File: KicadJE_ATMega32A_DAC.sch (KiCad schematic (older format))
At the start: 74 parts, among them J101 CV1, J102 CV2, J103 OUT1, J104 OUT2, J105 IN1, J106 IN2

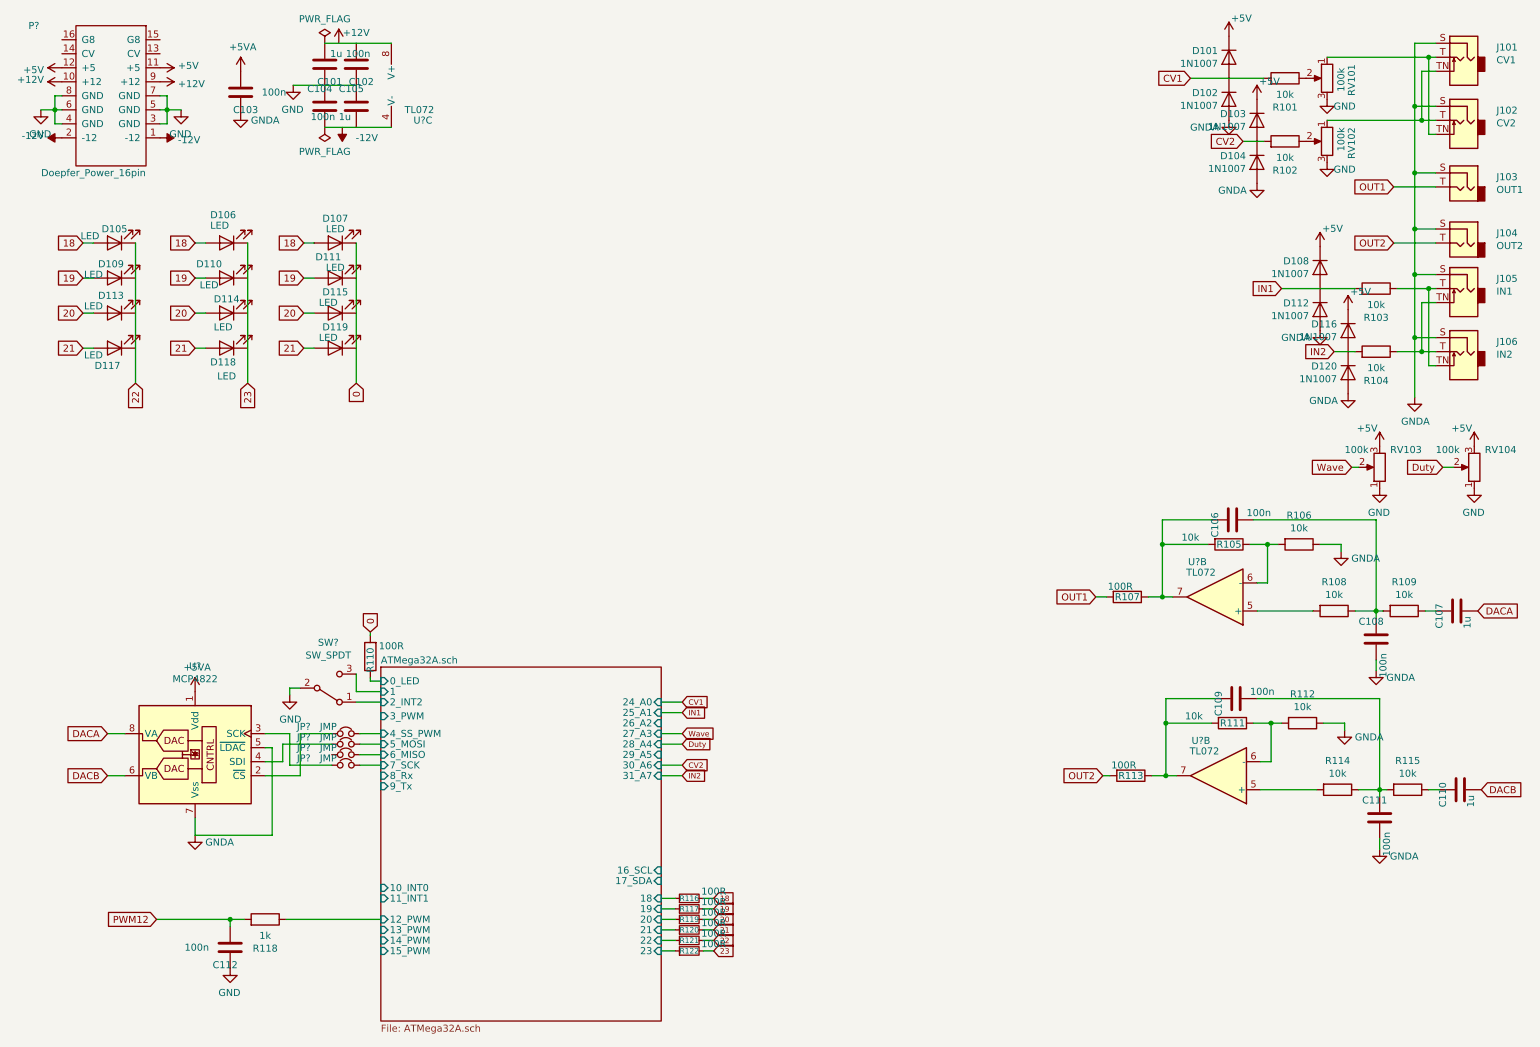
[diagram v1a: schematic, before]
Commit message: Intersheet cleanup
Footprints and cleanup naming on global labels between sheets
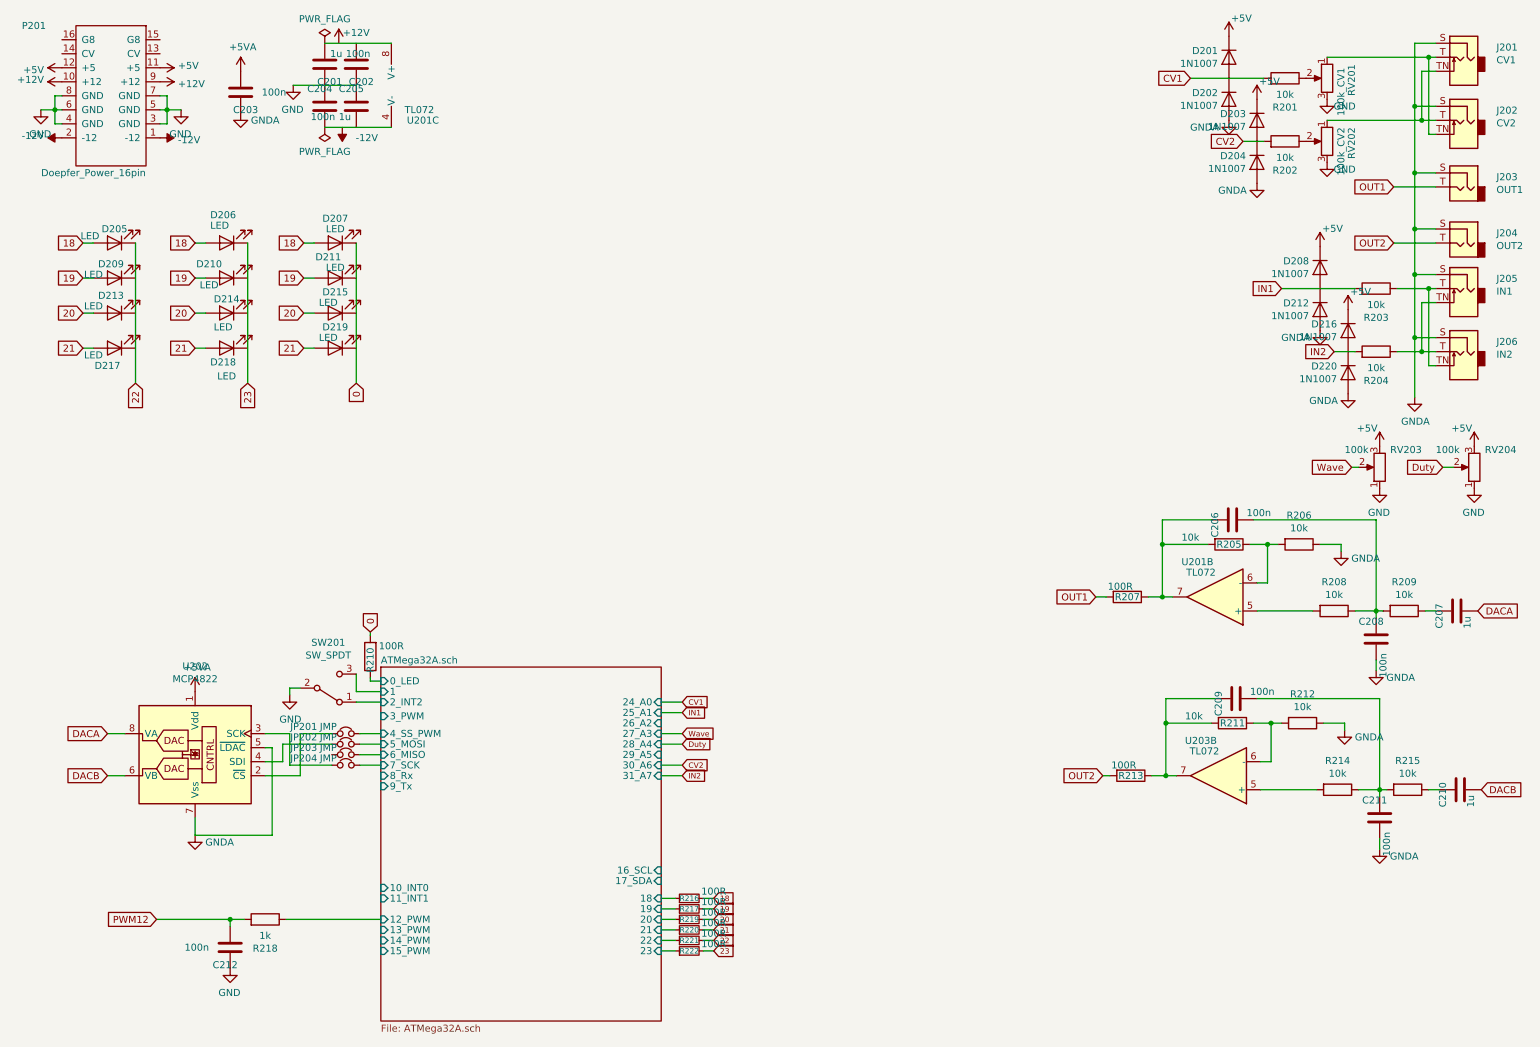
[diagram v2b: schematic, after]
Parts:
- RV201: renamed from RV101; value 100k -> 100k_CV1
- RV202: renamed from RV102; value 100k -> 100k_CV2
- SW201: renamed from SW?; footprint (none) -> AJ:SP1MS1
- U201, U202, U203: renamed from U?; footprint (none) -> AJ:AJ_SO-8_5.3x6.2mm_P1.27mm
- gave numbers to parts that had none: 6
- renumbered C101 to C201, C102 to C202, C103 to C203, C104 to C204, C105 to C205, C106 to C206, C107 to C207, C108 to C208, C109 to C209, C110 to C210, C111 to C211, C112 to C212, D101 to D201, D102 to D202, D103 to D203, D104 to D204, D105 to D205, D106 to D206, D107 to D207, D108 to D208, D109 to D209, D110 to D210, D111 to D211, D112 to D212, D113 to D213, D114 to D214, D115 to D215, D116 to D216, D117 to D217, D118 to D218, D119 to D219, D120 to D220, J101 to J201, J102 to J202, J103 to J203, J104 to J204, J105 to J205, J106 to J206, R101 to R201, R102 to R202, R103 to R203, R104 to R204, R105 to R205, R106 to R206, R107 to R207, R108 to R208, R109 to R209, R110 to R210, R111 to R211, R112 to R212, R113 to R213, R114 to R214, R115 to R215, R116 to R216, R117 to R217, R118 to R218, R119 to R219, R120 to R220, R121 to R221, R122 to R222, RV103 to RV203, RV104 to RV204

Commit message: LED Matrix ATMega32 rename
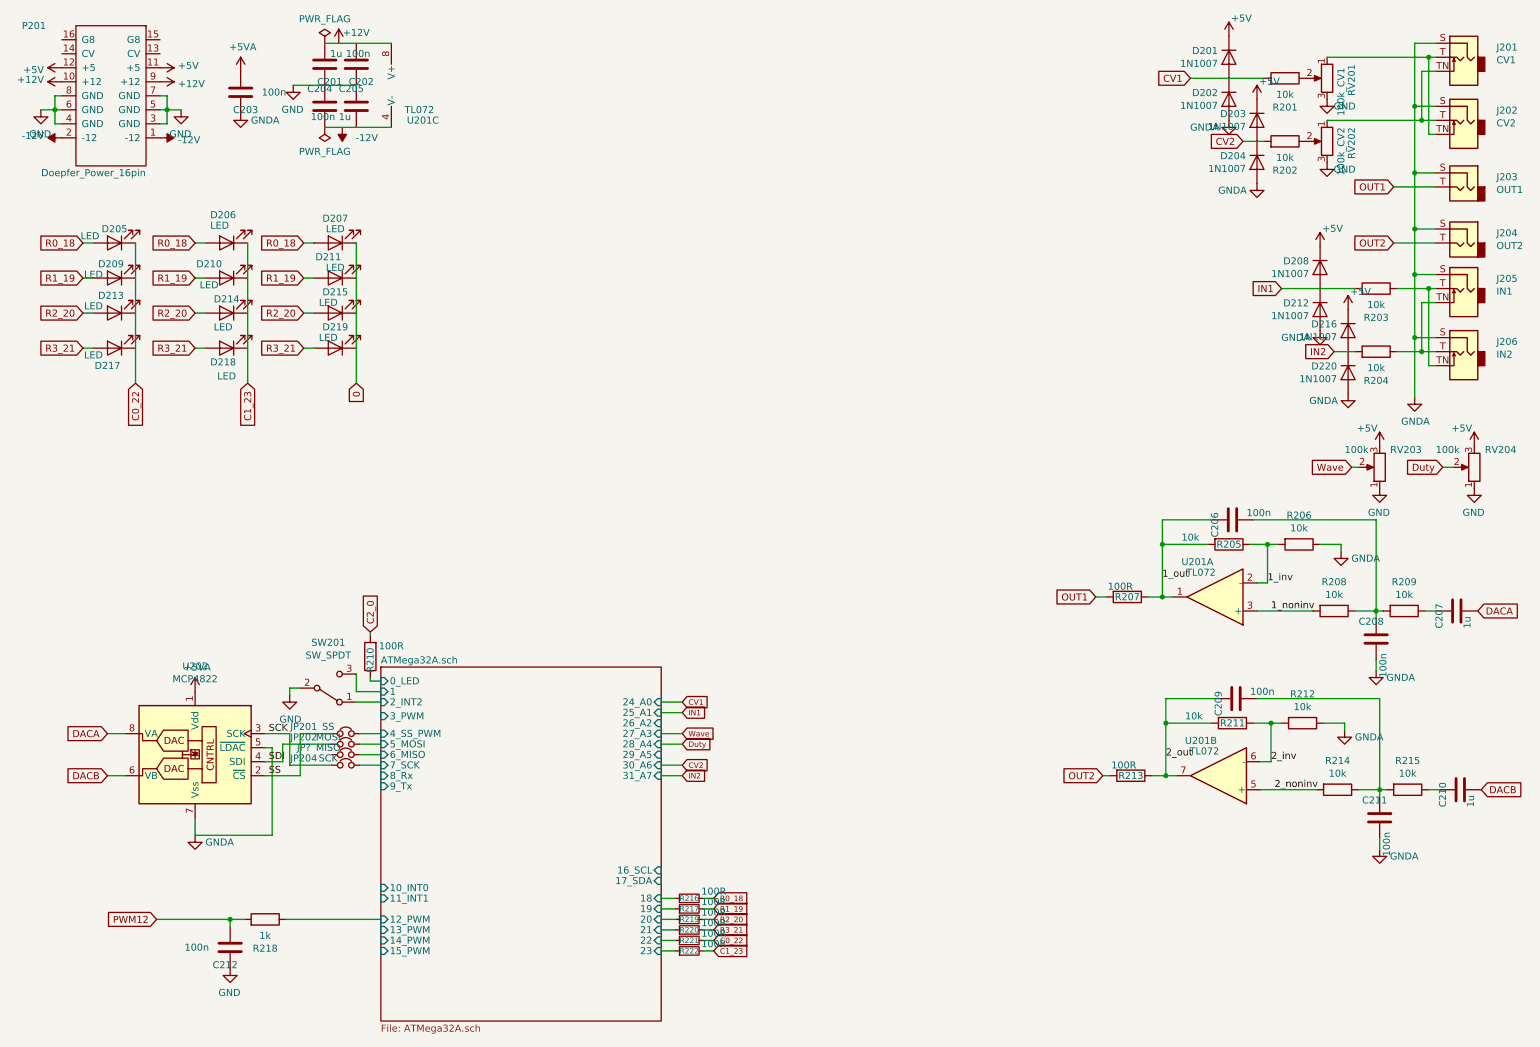
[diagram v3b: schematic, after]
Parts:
- removed JP203: JMP, Connector_PinSocket_2.54mm:PinSocket_1x02_P2.54mm_Vertical, symbol Device:Jumper_NC_Small
- added JP?: MISO, Connector_PinSocket_2.54mm:PinSocket_1x02_P2.54mm_Vertical, symbol Device:Jumper_NC_Small
- JP201: value JMP -> SS
- JP202: value JMP -> MOSI
- JP204: value JMP -> SCK
- renumbered U203 to U201
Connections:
- net 0: no longer R210.2
- net ATMega32A.sch/6_MISO: now also JP?.2
- net SS: now reaches JP201.1, U202.2 (~CS)
- net SCK: now reaches JP204.1, U202.3 (SCK)
- net SDI: now reaches JP202.1, U202.4 (SDI)
- net 2_noninv: now reaches R214.2, U201.5 (+)
- net 2_inv: now reaches R211.1, R212.2, U201.6 (-)
- net 2_out: now reaches C209.1, R211.2, R213.1, U201.7
- net 1_noninv: now reaches R208.2
- net 1_noninv: now also U201.3 (+); no longer U201.5 (+)
- net 1_inv: now reaches R205.1, R206.2
- net 1_inv: now also U201.2 (-); no longer U201.6 (-)
- net 1_out: now reaches C206.1, R205.2, R207.1
- net 1_out: now also U201.1; no longer U201.7
- net 18 renamed R0_18
- net 19 renamed R1_19
- net 20 renamed R2_20
- net 21 renamed R3_21
- net 22 renamed C0_22
- net 23 renamed C1_23
- new net C2_0: R210.2
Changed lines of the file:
@@
 OUT2
 Text GLabel 900  2075 0    50   Input ~ 0
-18
+R0_18
 Text GLabel 900  2325 0    50   Input ~ 0
-19
+R1_19
 Text GLabel 900  2575 0    50   Input ~ 0
-20
+R2_20
 Text GLabel 900  2825 0    50   Input ~ 0
-21
+R3_21
 Text GLabel 1275 3075 3    50   Input ~ 0
-22
+C0_22
 Text GLabel 2075 3075 3    50   Input ~ 0
-23
+C1_23
 Text GLabel 1425 6900 0    50   Input ~ 0
 PWM12
@@
 	0    1    -1   0
 $EndComp
-Text GLabel 1700 2575 0    50   Input ~ 0
-20
-Text GLabel 1700 2825 0    50   Input ~ 0
-21
-Text GLabel 1700 2325 0    50   Input ~ 0
-19
-Text GLabel 2475 2575 0    50   Input ~ 0
-20
-Text GLabel 2475 2825 0    50   Input ~ 0
-21
-Text GLabel 2475 2325 0    50   Input ~ 0
-19
-Text GLabel 1700 2075 0    50   Input ~ 0
-18
-Text GLabel 2475 2075 0    50   Input ~ 0
-18
 Wire Wire Line
 	10400 2300 10400 2750
@@
 P 2775 5800
 F 0 "JP204" H 2475 5850 50  0000 C CNN
-F 1 "JMP" H 2650 5850 50  0000 C CNN
+F 1 "SCK" H 2650 5850 50  0000 C CNN
 F 2 "Connector_PinSocket_2.54mm:PinSocket_1x02_P2.54mm_Vertical" H 2775 5800 50  0001 C CNN
 F 3 "~" H 2775 5800 50  0001 C CNN
 	1    2775 5800
-	1    0    0    -1
-$EndComp
-$Comp
-L Device:Jumper_NC_Small JP203
-U 1 1 5CF0FDB3
-P 2775 5725
-F 0 "JP203" H 2475 5775 50  0000 C CNN
-F 1 "JMP" H 2650 5775 50  0000 C CNN
-F 2 "Connector_PinSocket_2.54mm:PinSocket_1x02_P2.54mm_Vertical" H 2775 5725 50  0001 C CNN
-F 3 "~" H 2775 5725 50  0001 C CNN
-	1    2775 5725
 	1    0    0    -1
 $EndComp
@@
 P 2775 5650
 F 0 "JP202" H 2475 5700 50  0000 C CNN
-F 1 "JMP" H 2650 5700 50  0000 C CNN
+F 1 "MOSI" H 2650 5700 50  0000 C CNN
 F 2 "Connector_PinSocket_2.54mm:PinSocket_1x02_P2.54mm_Vertical" H 2775 5650 50  0001 C CNN
 F 3 "~" H 2775 5650 50  0001 C CNN
@@
 P 2775 5575
 F 0 "JP201" H 2475 5625 50  0000 C CNN
-F 1 "JMP" H 2650 5625 50  0000 C CNN
+F 1 "SS" H 2650 5625 50  0000 C CNN
 F 2 "Connector_PinSocket_2.54mm:PinSocket_1x02_P2.54mm_Vertical" H 2775 5575 50  0001 C CNN
 F 3 "~" H 2775 5575 50  0001 C CNN
@@
 Wire Wire Line
 	2875 5650 3025 5650
-Wire Wire Line
-	2875 5725 3025 5725
 Wire Wire Line
 	2875 5800 3025 5800
@@
 $EndComp
 $Comp
-L Amplifier_Operational:TL072 U203
+L Amplifier_Operational:TL072 U201
 U 2 1 5CF6156F
 P 9000 5875
-F 0 "U203" H 9125 5625 50  0000 C CNN
+F 0 "U201" H 9125 5625 50  0000 C CNN
 F 1 "TL072" H 9100 5700 50  0000 C CNN
 F 2 "AJ:AJ_SO-8_5.3x6.2mm_P1.27mm" H 9000 5875 50  0001 C CNN
@@
 $Comp
 L Amplifier_Operational:TL072 U201
-U 2 1 5D4DCC0D
+U 1 1 5D4DCC0D
 P 8975 4600
 F 0 "U201" H 9100 4350 50  0000 C CNN
@@
 F 2 "AJ:AJ_SO-8_5.3x6.2mm_P1.27mm" H 8975 4600 50  0001 C CNN
 F 3 "http://www.ti.com/lit/ds/symlink/tl071.pdf" H 8975 4600 50  0001 C CNN
-	2    8975 4600
+	1    8975 4600
 	-1   0    0    1
 $EndComp
@@
 Wire Wire Line
 	2850 5350 3025 5350
-Text GLabel 5400 6750 2    39   Input ~ 0
-18
-Text GLabel 5400 6825 2    39   Input ~ 0
-19
-Text GLabel 5400 6900 2    39   Input ~ 0
-20
-Text GLabel 5400 6975 2    39   Input ~ 0
-21
 Text GLabel 2950 4850 1    50   Input ~ 0
-0
+C2_0
 Text GLabel 5400 7050 2    39   Input ~ 0
-22
+C0_22
 Text GLabel 5400 7125 2    39   Input ~ 0
-23
+C1_23
 $Comp
 L Device:R R?
@@
 Wire Wire Line
 	2850 2075 2850 3075
+Text Label 9375 4700 0    50   ~ 0
+1_noninv
+Text Label 9400 5975 0    50   ~ 0
+2_noninv
+Text Label 9375 5775 0    50   ~ 0
+2_inv
+Text Label 9350 4500 0    50   ~ 0
+1_inv
+Text Label 8600 4475 0    50   ~ 0
+1_out
+Text Label 8625 5750 0    50   ~ 0
+2_out
+Text Label 2225 5875 0    50   ~ 0
+SS
+Text Label 2225 5775 0    50   ~ 0
+SDI
+Text Label 2225 5575 0    50   ~ 0
+SCK
+$Comp
+L Device:Jumper_NC_Small JP?
+U 1 1 5D23F56B
+P 2775 5725
+F 0 "JP?" H 2475 5775 50  0000 C CNN
+F 1 "MISO" H 2650 5775 50  0000 C CNN
+F 2 "Connector_PinSocket_2.54mm:PinSocket_1x02_P2.54mm_Vertical" H 2775 5725 50  0001 C CNN
+F 3 "~" H 2775 5725 50  0001 C CNN
+	1    2775 5725
+	1    0    0    -1
+$EndComp
+Wire Wire Line
+	2875 5725 3025 5725
+Text GLabel 1700 2075 0    50   Input ~ 0
+R0_18
+Text GLabel 1700 2325 0    50   Input ~ 0
+R1_19
+Text GLabel 1700 2575 0    50   Input ~ 0
+R2_20
+Text GLabel 1700 2825 0    50   Input ~ 0
+R3_21
+Text GLabel 2475 2075 0    50   Input ~ 0
+R0_18
+Text GLabel 2475 2325 0    50   Input ~ 0
+R1_19
+Text GLabel 2475 2575 0    50   Input ~ 0
+R2_20
+Text GLabel 2475 2825 0    50   Input ~ 0
+R3_21
+Text GLabel 5400 6750 2    39   Input ~ 0
+R0_18
+Text GLabel 5400 6825 2    39   Input ~ 0
+R1_19
+Text GLabel 5400 6900 2    39   Input ~ 0
+R2_20
+Text GLabel 5400 6975 2    39   Input ~ 0
+R3_21
 $EndSCHEMATC
